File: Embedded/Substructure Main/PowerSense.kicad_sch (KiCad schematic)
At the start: 8 parts, among them U6 INA220AIDGSR

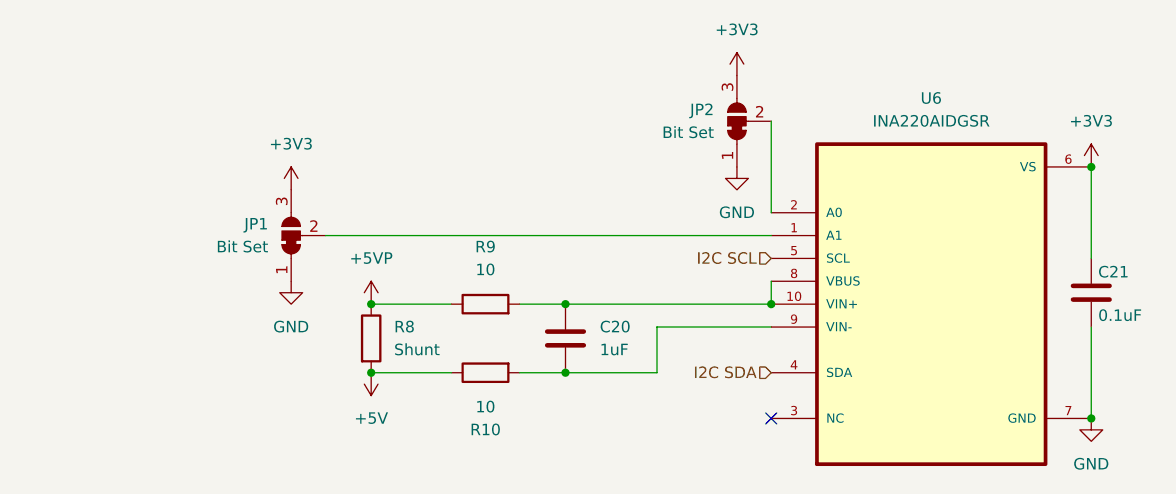
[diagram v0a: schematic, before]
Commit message: Added LDOs and Modified Component Names
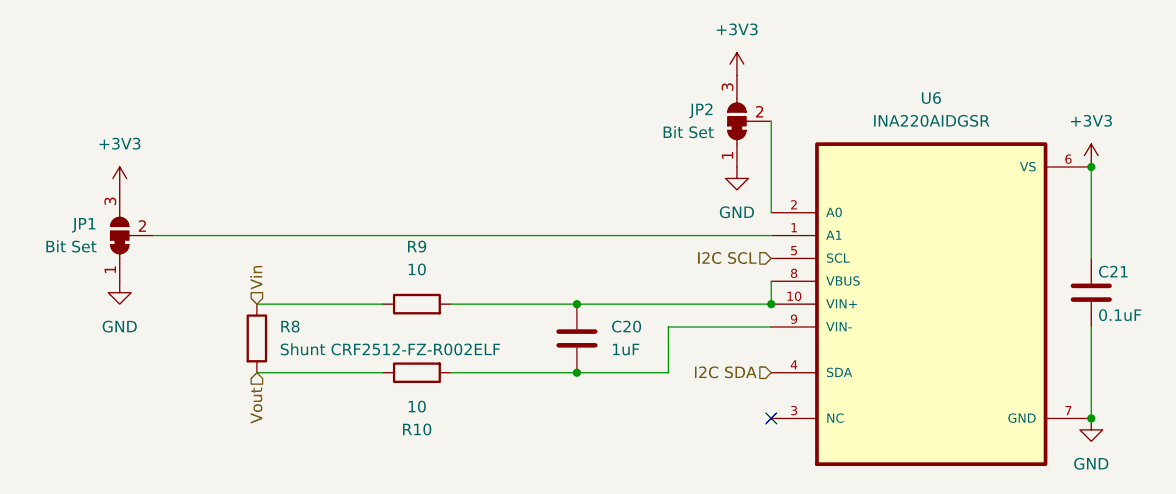
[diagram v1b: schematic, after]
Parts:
- R8: value Shunt -> Shunt CRF2512-FZ-R002ELF
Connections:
- net +5V renamed Vout
- net +5VP renamed Vin
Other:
- moved on the sheet: C20, JP1, R10, R8, R9

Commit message: Added Sensored V2 Board
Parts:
- renumbered C20 to C28, C21 to C29, U6 to U10
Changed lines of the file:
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@@
 		(dnp no)
 		(fields_autoplaced yes)
-		(property "Reference" "#PWR051"
+		(property "Reference" "#PWR076"
 			(at 118.11 59.69 0)
 			(effects
@@
 			(project "Substructure Main"
 				(path "/dda3f9ed-866a-496e-a4f2-d6745d13652e/51082c6a-6569-4ea1-8d6d-16d74ca2203a"
-					(reference "#PWR051")
+					(reference "#PWR076")
 					(unit 1)
 				)
@@
 		(dnp no)
 		(fields_autoplaced yes)
-		(property "Reference" "#PWR029"
+		(property "Reference" "#PWR073"
 			(at 49.53 59.69 0)
 			(effects
@@
 			(project "Substructure Main"
 				(path "/dda3f9ed-866a-496e-a4f2-d6745d13652e/51082c6a-6569-4ea1-8d6d-16d74ca2203a"
-					(reference "#PWR029")
+					(reference "#PWR073")
 					(unit 1)
 				)
@@
 		(dnp no)
 		(fields_autoplaced yes)
-		(property "Reference" "C20"
+		(property "Reference" "C28"
 			(at 104.14 71.1199 0)
 			(effects
@@
 			(project "Substructure Main"
 				(path "/dda3f9ed-866a-496e-a4f2-d6745d13652e/51082c6a-6569-4ea1-8d6d-16d74ca2203a"
-					(reference "C20")
+					(reference "C28")
 					(unit 1)
 				)
@@
 		(dnp no)
 		(fields_autoplaced yes)
-		(property "Reference" "U6"
+		(property "Reference" "U10"
 			(at 139.7 45.72 0)
 			(effects
@@
 			(project "Substructure Main"
 				(path "/dda3f9ed-866a-496e-a4f2-d6745d13652e/51082c6a-6569-4ea1-8d6d-16d74ca2203a"
-					(reference "U6")
+					(reference "U10")
 					(unit 1)
 				)
@@
 		(dnp no)
 		(fields_autoplaced yes)
-		(property "Reference" "#PWR052"
+		(property "Reference" "#PWR077"
 			(at 157.48 57.15 0)
 			(effects
@@
 			(project "Substructure Main"
 				(path "/dda3f9ed-866a-496e-a4f2-d6745d13652e/51082c6a-6569-4ea1-8d6d-16d74ca2203a"
-					(reference "#PWR052")
+					(reference "#PWR077")
 					(unit 1)
 				)
@@
 		(on_board yes)
 		(dnp no)
-		(property "Reference" "C21"
+		(property "Reference" "C29"
 			(at 158.242 65.024 0)
 			(effects
@@
 			(project "Substructure Main"
 				(path "/dda3f9ed-866a-496e-a4f2-d6745d13652e/51082c6a-6569-4ea1-8d6d-16d74ca2203a"
-					(reference "C21")
+					(reference "C29")
 					(unit 1)
 				)
@@
 		(dnp no)
 		(fields_autoplaced yes)
-		(property "Reference" "#PWR050"
+		(property "Reference" "#PWR075"
 			(at 118.11 46.99 0)
 			(effects
@@
 			(project "Substructure Main"
 				(path "/dda3f9ed-866a-496e-a4f2-d6745d13652e/51082c6a-6569-4ea1-8d6d-16d74ca2203a"
-					(reference "#PWR050")
+					(reference "#PWR075")
 					(unit 1)
 				)
@@
 		(dnp no)
 		(fields_autoplaced yes)
-		(property "Reference" "#PWR047"
+		(property "Reference" "#PWR074"
 			(at 49.53 72.39 0)
 			(effects
@@
 			(project "Substructure Main"
 				(path "/dda3f9ed-866a-496e-a4f2-d6745d13652e/51082c6a-6569-4ea1-8d6d-16d74ca2203a"
-					(reference "#PWR047")
+					(reference "#PWR074")
 					(unit 1)
 				)
@@
 		(dnp no)
 		(fields_autoplaced yes)
-		(property "Reference" "#PWR053"
+		(property "Reference" "#PWR078"
 			(at 157.48 87.63 0)
 			(effects
@@
 			(project "Substructure Main"
 				(path "/dda3f9ed-866a-496e-a4f2-d6745d13652e/51082c6a-6569-4ea1-8d6d-16d74ca2203a"
-					(reference "#PWR053")
-					(unit 1)
-				)
+					(reference "#PWR078")
+					(unit 1)
+				)
